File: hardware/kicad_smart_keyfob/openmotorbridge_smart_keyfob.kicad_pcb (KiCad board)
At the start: 2 copper layers, 38 x 19 mm, 25 parts, among them M1 LRA_MOTOR_PADS, SW1 BTN_ARM, SW2 BTN_SOS, U1 nRF52840-QIAA, U2 SX1262IMLTRT, U3 DRV2605LDGSR, U4 BQ51003YFPR, U5 BQ25100YFPR, Y1 32.000MHz, Y2 32.768kHz, Y3 32MHz_TCXO

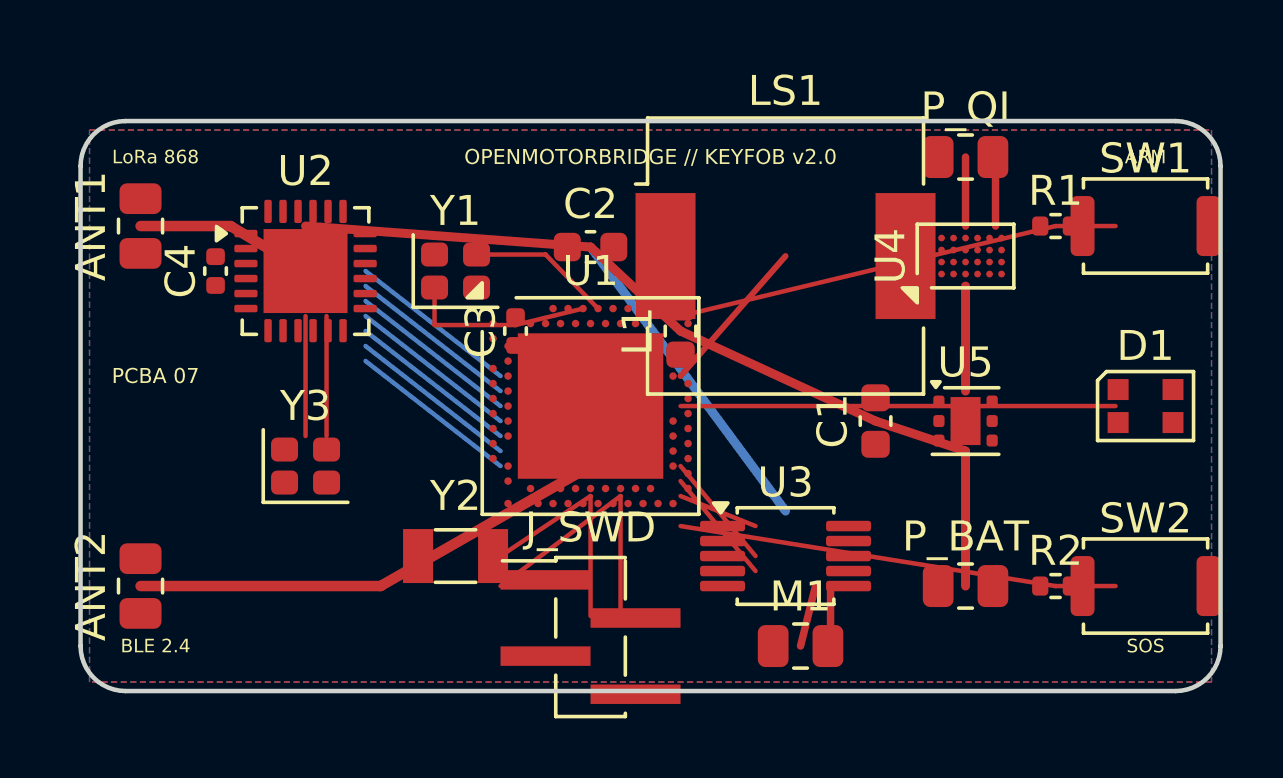
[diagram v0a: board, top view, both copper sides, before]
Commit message: feat(hardware,docs): integrate feedback, update PCBA 07 packages, fix CAD cross-section render, and harmonize DE/EN chapters
- Hardware & PCB: preserve user placement & routing for PCBA 07, update JLCPCB manufacturing packages, and generate high-res 3D render
- CAD & Renders: fix OpenSCAD use directive and CGAL render for poka-yoke cross-section (fig 8.7); rebuild all 56 STLs and 30 3D PNG renders
- Documentation: update chapters 01, 04, 05, 07, 08, 15, and 16 across German and English with strict 1:1 symmetry
  * Ch 01: replace CR2032 remote with Front-Node PCBA 05 hardwired PTT + Smart-Keyfob PCBA 07 LiPo
  * Ch 04: clarify default external 2.4 GHz antenna and Murata MM8030 bypass for GNSS/LoRa
  * Ch 05: update section 6 to decentralized power monitoring (Front-Node 12V + Keyfob LiPo fuel gauge)
  * Ch 07: document TLP222A optocoupler role, 4 discrete independent actuators on J_ACT, and modular J2 harness variants
  * Ch 08: harmonize magnetic lock, 4 discrete actuators (3 top + 1 angled side for Sena; 3 buttons + wheel-click for Cardo), blind cartridge latching, and merge Harley touring kits
  * Ch 15 & 16: update Category E BOM for J_ACT harness, J2 modular harness, and 4x solenoids; reclassify 90 deg USB cable as legacy
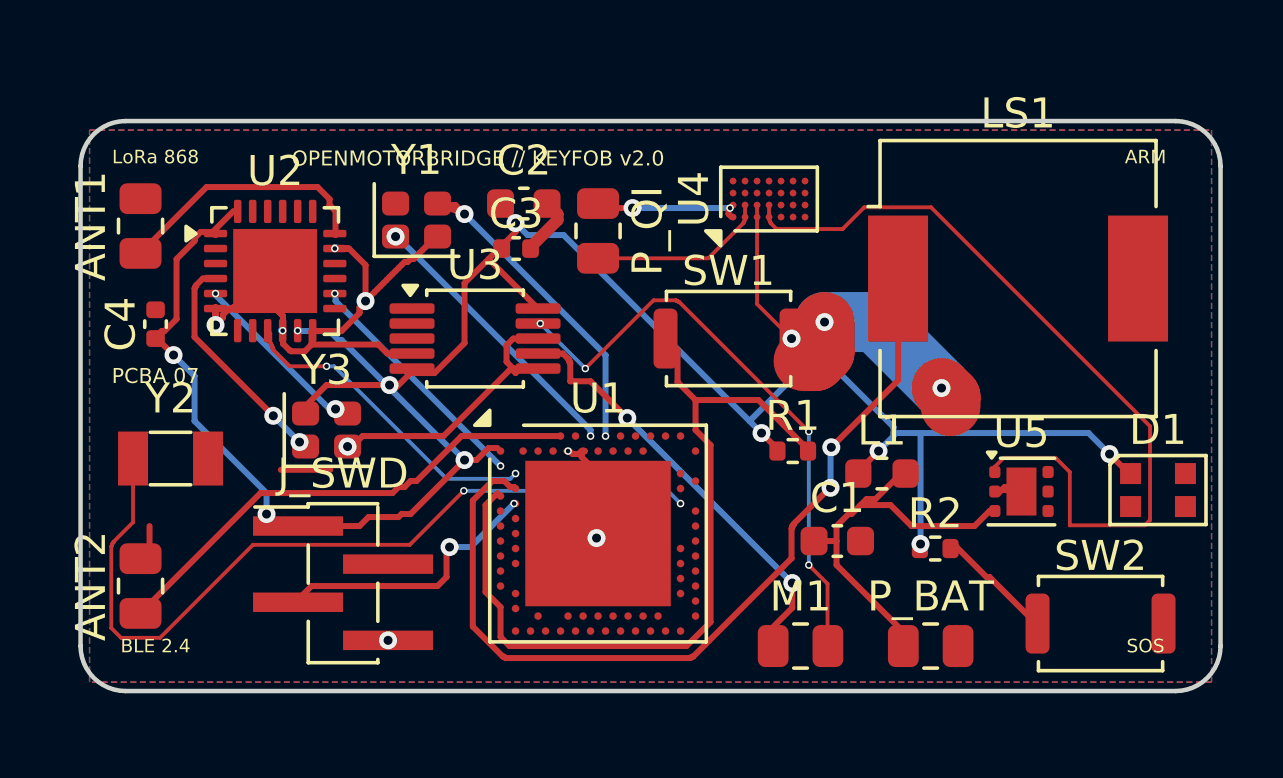
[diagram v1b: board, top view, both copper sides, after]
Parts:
- moved SW1 14.4 mm to (121.6, 77.2)
- moved U3 12.6 mm to (113.2, 77.2)
- moved P_QI 12.5 mm to (117.2, 73.7), turned to -90 degrees
- moved R1 11.5 mm to (123.7, 81.0)
- moved Y2 10.0 mm to (103.0, 81.2)
- moved J_SWD 8.44 mm to (108.8, 85.4)
- moved L1 8.22 mm to (126.7, 81.8), turned to 0 degrees
- moved LS1 7.79 mm to (131.2, 75.2)
- moved U4 6.82 mm to (123.0, 72.6)
- moved U1 4.26 mm to (117.2, 83.8)
- moved R2 4.20 mm to (128.5, 84.2)
- moved C1 4.20 mm to (125.2, 84.0), turned to 0 degrees
- moved U5 3.00 mm to (131.4, 82.3)
- moved D1 2.83 mm to (135.9, 82.3)
- moved C3 2.75 mm to (114.5, 74.2), turned to 0 degrees
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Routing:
- net GND: track 0.00 -> 52.2 mm, vias 0 -> 11
- net VCC_3V3: track 24.6 -> 75.6 mm, vias 0 -> 10
- net BUZZER_PWM: track 5.32 -> 29.2 mm, vias 0 -> 2
- net VCC_QI_5V: track 3.50 -> 27.3 mm
- net RTC2: track 5.00 -> 27.3 mm, vias 0 -> 2
- net LRA_NEG: track 2.00 -> 19.8 mm, vias 0 -> 4
- net LED_DATA: track 14.5 -> 0.00 mm
- net LRA_POS: track 2.06 -> 14.6 mm, vias 0 -> 2
- net BTN_ARM_N: track 14.9 -> 26.7 mm
- net BTN_SOS_N: track 14.7 -> 4.08 mm
- net XTAL2: track 4.81 -> 11.4 mm, vias 0 -> 2
- net LORA_RESET: track 5.70 -> 0.00 mm
- net LORA_NSS: track 5.70 -> 0.00 mm
- net LORA_MOSI: track 5.70 -> 0.00 mm
- net LORA_MISO: track 5.70 -> 0.00 mm
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
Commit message: hardware(pcb): synchronize 5-PCBA lineup with v9.6 All-UWB architecture
- PCBA 01 (Central Box): replace obsolete 26-pin IDC header with 12-pin Deutsch DTM-12 header (exact 12-pin net mapping), add 38.4MHz UWB crystal on B.Cu, update silkscreen and schematic
- PCBA 05 (Front Node): place Qorvo DW3110 + U.FL + crystal on B.Cu; place u-blox SAM-M10Q GNSS + Knowles MEMS mic on F.Cu
- PCBA 03 (Pod Cartridge): replace obsolete 6-pin dock socket with PAD1/PAD2 DC spring contact pads; place DW3110 + U.FL on B.Cu
- PCBA 08 (Radar Sub-MCU): update J1 to 2-pin 12V automotive power connector; place DW3110 + U.FL on B.Cu
- PCBA 07 (Smart Keyfob): replace solder pads with 2-pin JST-ACH SMD header (J_QI) for solderless Qi coil connection
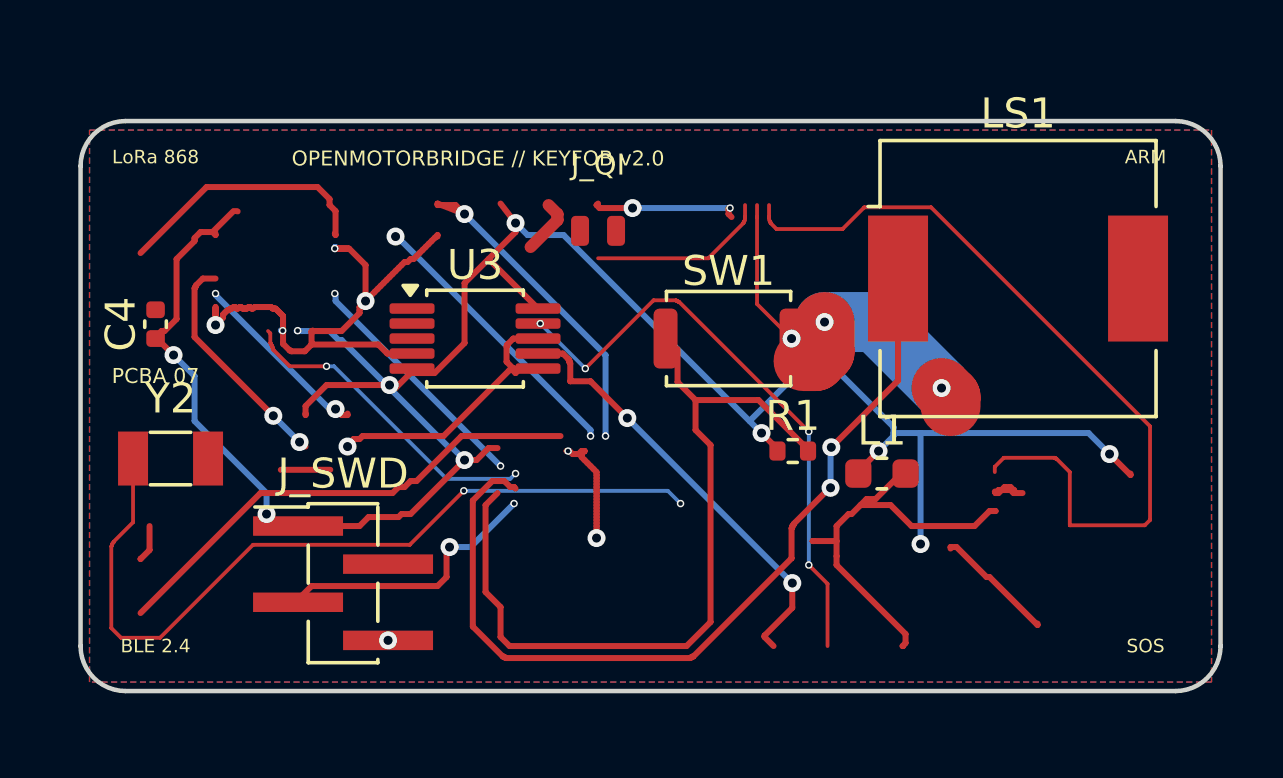
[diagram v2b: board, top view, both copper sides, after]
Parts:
- removed ANT1: 868MHz_CHIP_ANT, R_0805_2012Metric
- removed ANT2: 2.4GHz_BLE_ANT, R_0805_2012Metric
- removed C1: 10uF_VBAT, C_0603_1608Metric
- removed C2: 10uF_3V3, C_0603_1608Metric
- removed C3: 100nF_MCU, C_0402_1005Metric
- removed D1: WS2812B-2020, LED_WS2812B-2020_PLCC4_2.0x2.0mm
- removed M1: LRA_MOTOR_PADS, R_0805_2012Metric
- removed P_BAT: LIPO_BAT_PADS, R_0805_2012Metric
- removed P_QI: QI_COIL_PADS, R_0805_2012Metric
- removed R2: 10k_PULLUP, R_0402_1005Metric
- removed SW2: BTN_SOS, SW_Push_SPST_NO_Alps_SKRK
- removed U1: nRF52840-QIAA, Nordic_AQFN-73-1EP_7x7mm_P0.5mm
- removed U2: SX1262IMLTRT, QFN-24-1EP_4x4mm_P0.5mm_EP2.8x2.8mm
- removed U4: BQ51003YFPR, Texas_DSBGA-28_1.9x3mm_Layout4x7_P0.4mm
- removed U5: BQ25100YFPR, WSON-6-1EP_2x2mm_P0.65mm_EP1x1.6mm
- removed Y1: 32.000MHz, Crystal_SMD_2016-4Pin_2.0x1.6mm
- removed Y3: 32MHz_TCXO, Crystal_SMD_2016-4Pin_2.0x1.6mm
- added J_QI: QI_COIL_ACH_2P, Connector_JST:JST_ACH_BM02B-ACHSS-GAN-ETF_1x02-1MP_P1.20mm_Vertical, F.Cu at (117.2, 73.7)

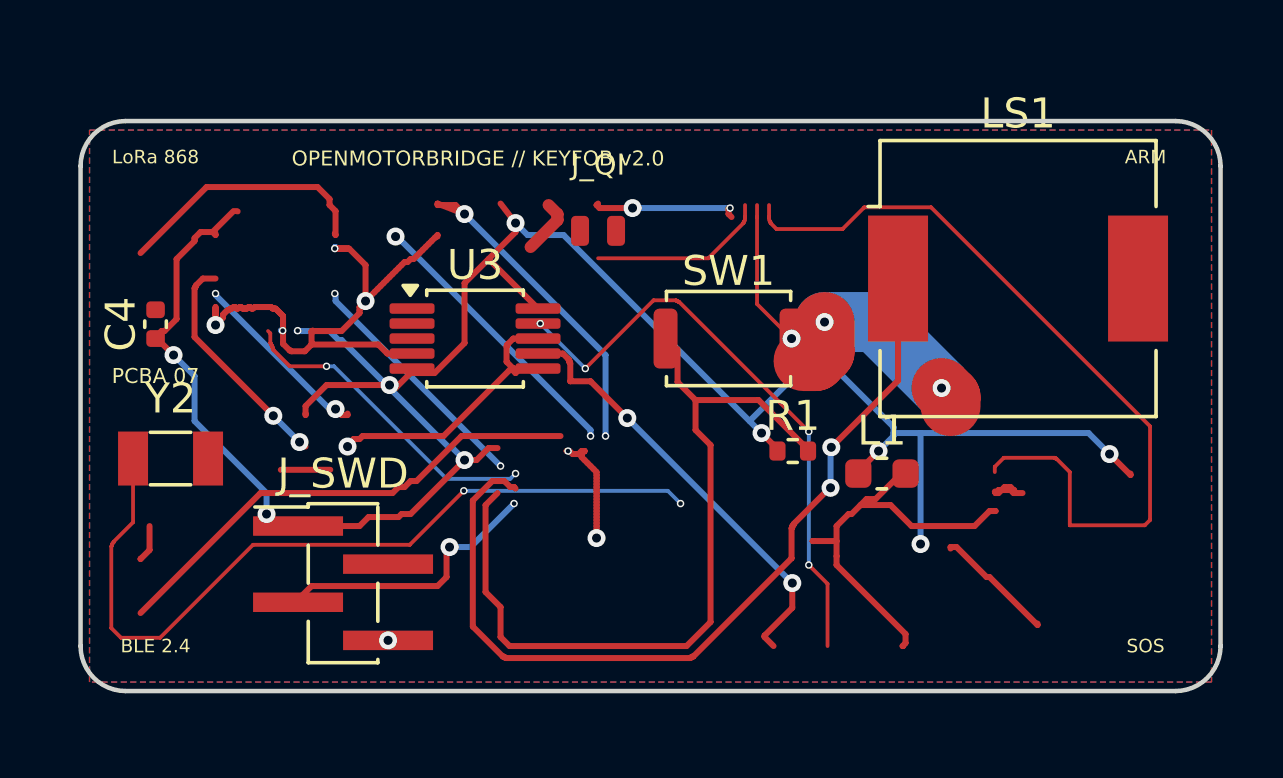
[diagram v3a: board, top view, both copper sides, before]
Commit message: hardware(front-node): remove misplaced onboard ublox SAM-M10Q footprint; cluster connects externally via J12 Qwiic
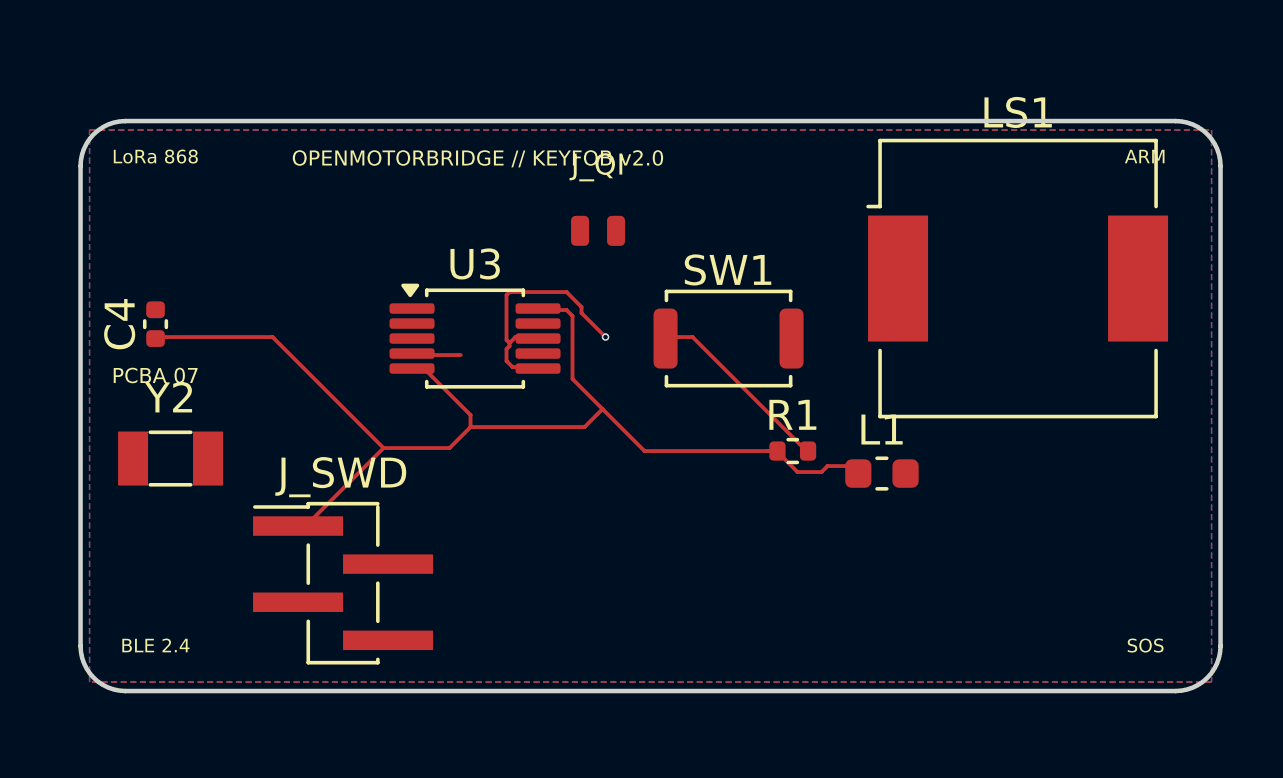
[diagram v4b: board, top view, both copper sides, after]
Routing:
- net GND: track 52.2 -> 10.3 mm, vias 11 -> 1
- net VCC_3V3: track 75.6 -> 38.8 mm, vias 10 -> 0
- net BUZZER_PWM: track 29.2 -> 0.00 mm, vias 2 -> 0
- net VCC_QI_5V: track 27.3 -> 0.00 mm
- net RTC2: track 27.3 -> 0.00 mm, vias 2 -> 0
- net BTN_ARM_N: track 26.7 -> 6.37 mm
- net LRA_NEG: track 19.8 -> 0.00 mm, vias 4 -> 0
- net BLE_ANT_50R: track 16.4 -> 0.00 mm
- net LRA_POS: track 14.6 -> 0.00 mm, vias 2 -> 0
- net VBAT: track 13.9 -> 0.00 mm
- net XTAL2: track 11.4 -> 0.00 mm, vias 2 -> 0
- net LORA_DIO1: track 10.6 -> 0.00 mm, vias 2 -> 0
- net XTAL1: track 9.39 -> 0.00 mm, vias 2 -> 0
- net SWDCLK: track 8.98 -> 0.00 mm, vias 2 -> 0
- net LORA_ANT_50R: track 8.72 -> 0.00 mm
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
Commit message: hardware(pcba): complete thorough audit across cartridge, front-node, fob, and radar
- PCBA 01 (Zentralbox): Verified MicroSD on B.Cu, edge clearance, DTM-12 intact
- PCBA 03 (Cartridge): Verified ES8388 Codec, DW3110 UWB, 0 overlaps, 0 shorts
- PCBA 05 (Front-Node): Verified DW3110 UWB, SAM-M10Q Qwiic, dual SW3526 PD, 0 collisions
- PCBA 07 (Smart Keyfob): Recovered truncated components (nRF52840, SX1262, BQ51003, BQ25100), replaced P_QI with pure SMD JST-ACH header, DRC clean
- PCBA 08 (Radar Sub-MCU): Restored missing J2 4-pin radar header at (144, 120) with clean power bypass and verified RX/TX unrouted ratsnest endpoints for manual user routing
- Docs & CAD: Removed XXX annotations, synchronized 2-wire DC harness and Sub-MCU autonomous TTC architecture, updated 3D renders across all boards
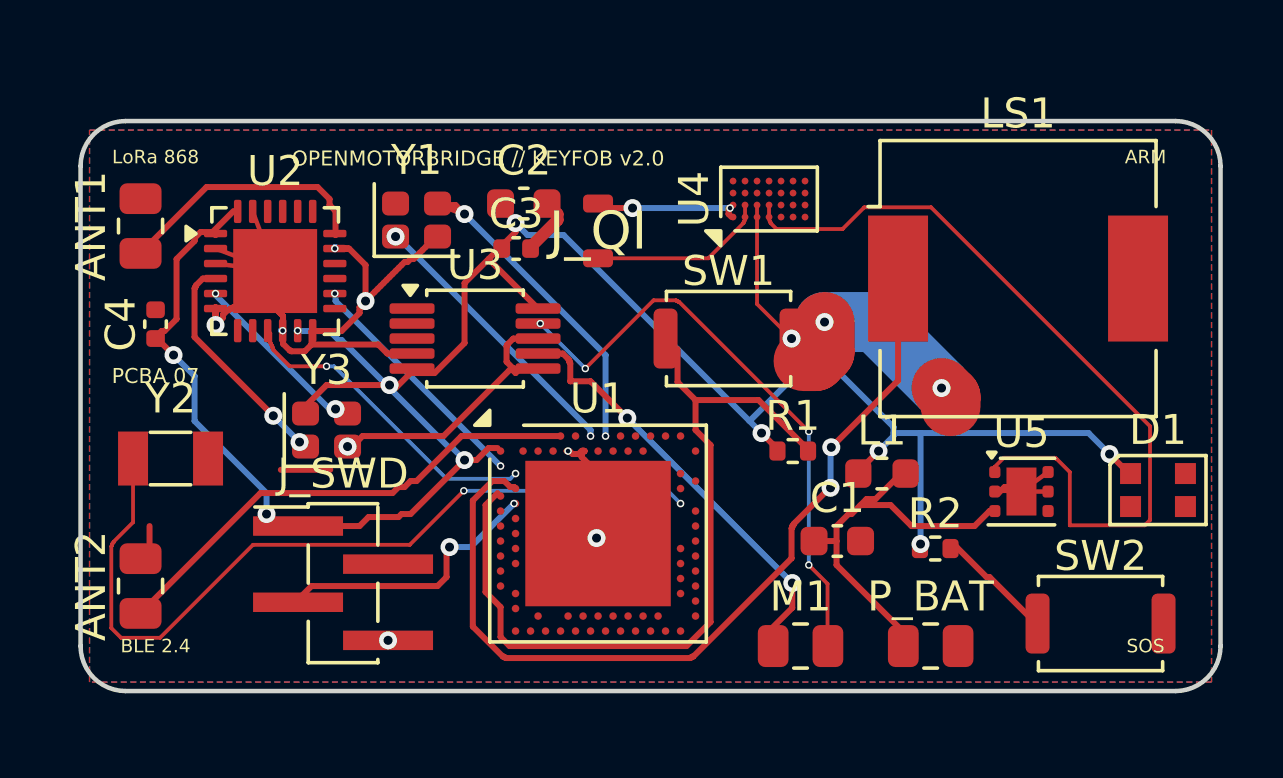
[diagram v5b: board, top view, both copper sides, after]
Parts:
- removed the J_QI at (117.2, 73.7)
- added ANT1: 868MHz_CHIP_ANT, R_0805_2012Metric, F.Cu at (102.0, 73.5)
- added ANT2: 2.4GHz_BLE_ANT, R_0805_2012Metric, F.Cu at (102.0, 85.5)
- added C1: 10uF_VBAT, C_0603_1608Metric, F.Cu at (125.2, 84.0)
- added C2: 10uF_3V3, C_0603_1608Metric, F.Cu at (114.8, 72.8)
- added C3: 100nF_MCU, C_0402_1005Metric, F.Cu at (114.5, 74.2)
- added D1: WS2812B-2020, LED_WS2812B-2020_PLCC4_2.0x2.0mm, F.Cu at (135.9, 82.3)
- added J_QI: QI_COIL_ACH_2P, , F.Cu at (117.2, 73.7)
- added M1: LRA_MOTOR_PADS, R_0805_2012Metric, F.Cu at (124.0, 87.5)
- added P_BAT: LIPO_BAT_PADS, R_0805_2012Metric, F.Cu at (128.3, 87.5)
- added R2: 10k_PULLUP, R_0402_1005Metric, F.Cu at (128.5, 84.2)
- added SW2: BTN_SOS, SW_Push_SPST_NO_Alps_SKRK, F.Cu at (134.0, 86.8)
- added U1: nRF52840-QIAA, Nordic_AQFN-73-1EP_7x7mm_P0.5mm, F.Cu at (117.2, 83.8)
- added U2: SX1262IMLTRT, QFN-24-1EP_4x4mm_P0.5mm_EP2.8x2.8mm, F.Cu at (106.5, 75.0)
- added U4: BQ51003YFPR, Texas_DSBGA-28_1.9x3mm_Layout4x7_P0.4mm, F.Cu at (123.0, 72.6)
- added U5: BQ25100YFPR, WSON-6-1EP_2x2mm_P0.65mm_EP1x1.6mm, F.Cu at (131.4, 82.3)
- added Y1: 32.000MHz, Crystal_SMD_2016-4Pin_2.0x1.6mm, F.Cu at (111.2, 73.3)
- added Y3: 32MHz_TCXO, Crystal_SMD_2016-4Pin_2.0x1.6mm, F.Cu at (108.2, 80.3)
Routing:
- net GND: track 10.3 -> 60.5 mm, vias 1 -> 11
- net VCC_3V3: track 38.8 -> 75.6 mm, vias 0 -> 10
- net BUZZER_PWM: track 0.00 -> 29.2 mm, vias 0 -> 2
- net VCC_QI_5V: track 0.00 -> 27.3 mm
- net RTC2: track 0.00 -> 27.3 mm, vias 0 -> 2
- net BTN_ARM_N: track 6.37 -> 26.7 mm
- net LRA_NEG: track 0.00 -> 19.8 mm, vias 0 -> 4
- net BLE_ANT_50R: track 0.00 -> 16.4 mm
- net LRA_POS: track 0.00 -> 14.6 mm, vias 0 -> 2
- net VBAT: track 0.00 -> 13.9 mm
- net XTAL2: track 0.00 -> 11.4 mm, vias 0 -> 2
- net LORA_DIO1: track 0.00 -> 10.6 mm, vias 0 -> 2
- net XTAL1: track 0.00 -> 9.39 mm, vias 0 -> 2
- net SWDCLK: track 0.00 -> 8.98 mm, vias 0 -> 2
- net LORA_ANT_50R: track 0.00 -> 8.72 mm
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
